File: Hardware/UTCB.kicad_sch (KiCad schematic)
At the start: 28 parts

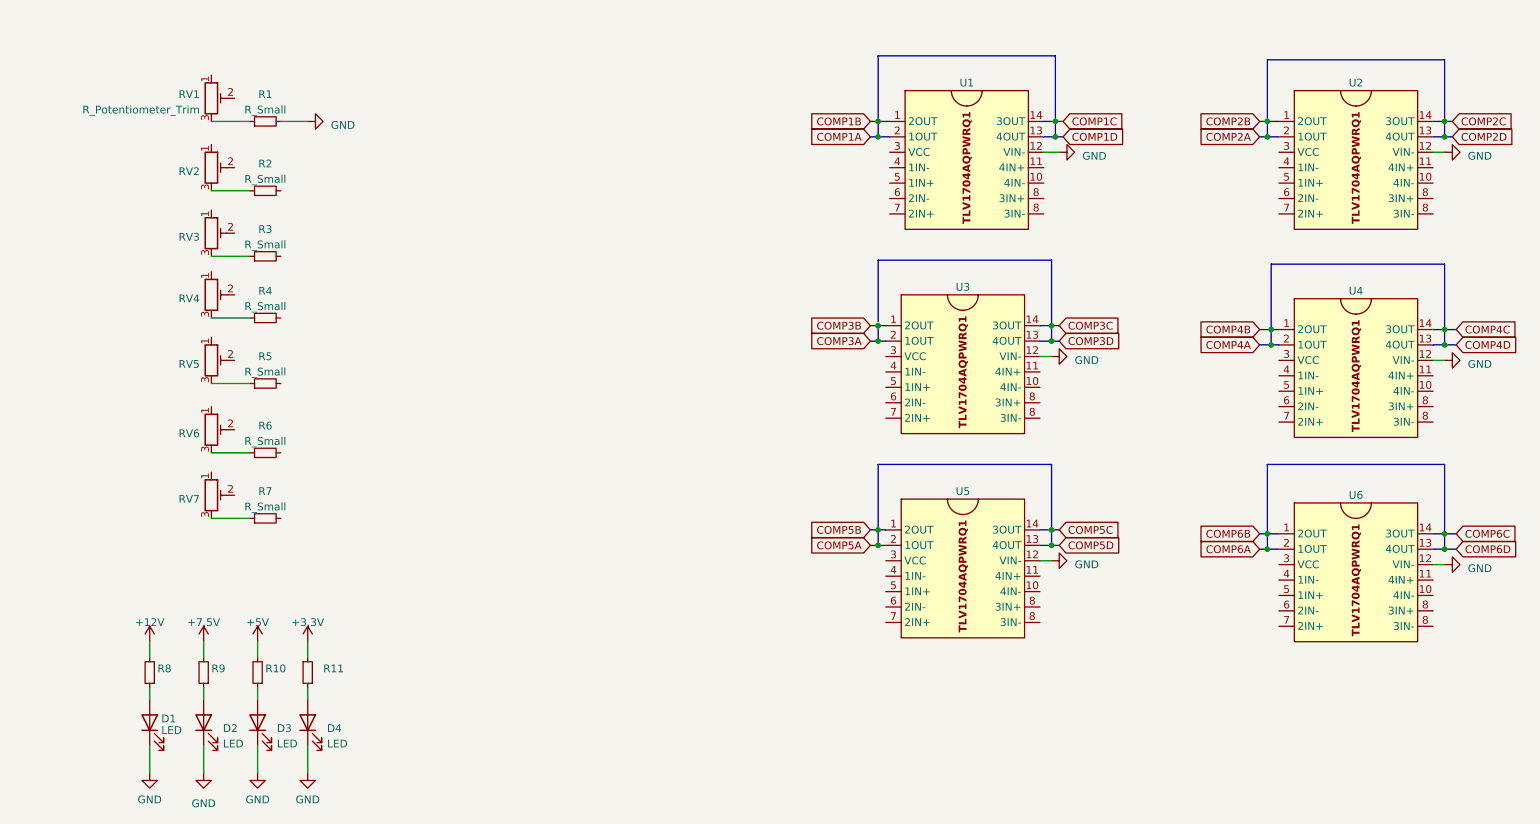
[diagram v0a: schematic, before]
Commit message: Added some changes for the logic switching circuitry. Will be adding thyristor or cascaded bjt configuration for various lighting types for each logic level
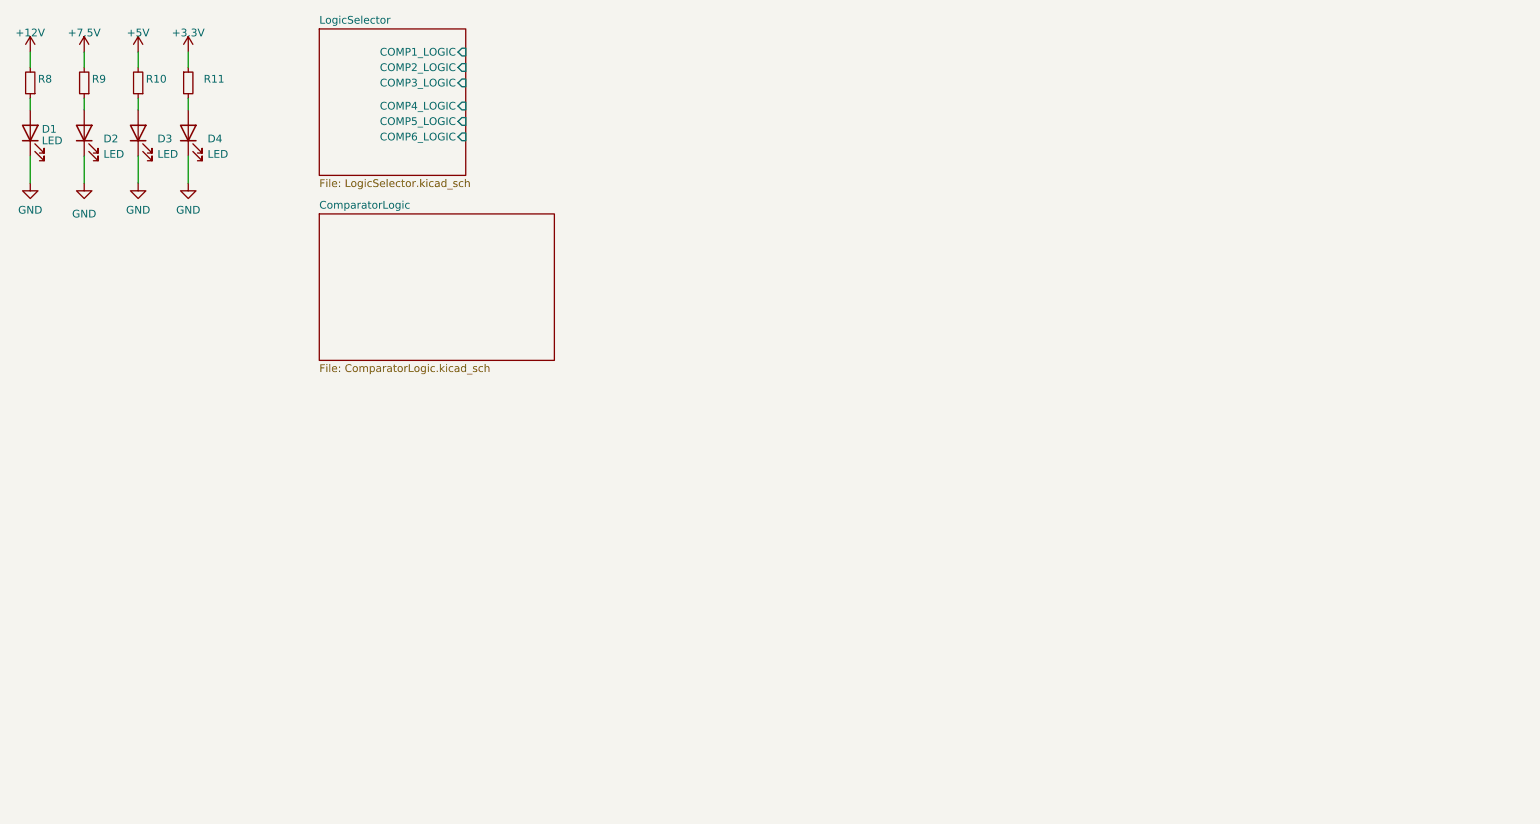
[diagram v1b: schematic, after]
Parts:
- removed R1, R2, R3, R4, R5, R6, R7: R_Small, symbol Device:R_Small
- removed RV1, RV2, RV3, RV4, RV5, RV6, RV7: R_Potentiometer_Trim, symbol Device:R_Potentiometer_Trim
- removed U1, U2, U3, U4, U5, U6: ~, Package_SO:HTSSOP-14-1EP_4.4x5mm_P0.65mm_EP3.4x5mm_Mask3x3.1mm, symbol ComparatorICs:TLV1704AQPWRQ1_
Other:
- added sheet ComparatorLogic (ComparatorLogic.kicad_sch)
- added sheet LogicSelector (LogicSelector.kicad_sch)
- moved on the sheet: D1, D2, D3, D4, R10, R11, R8, R9

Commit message: Added 3D models
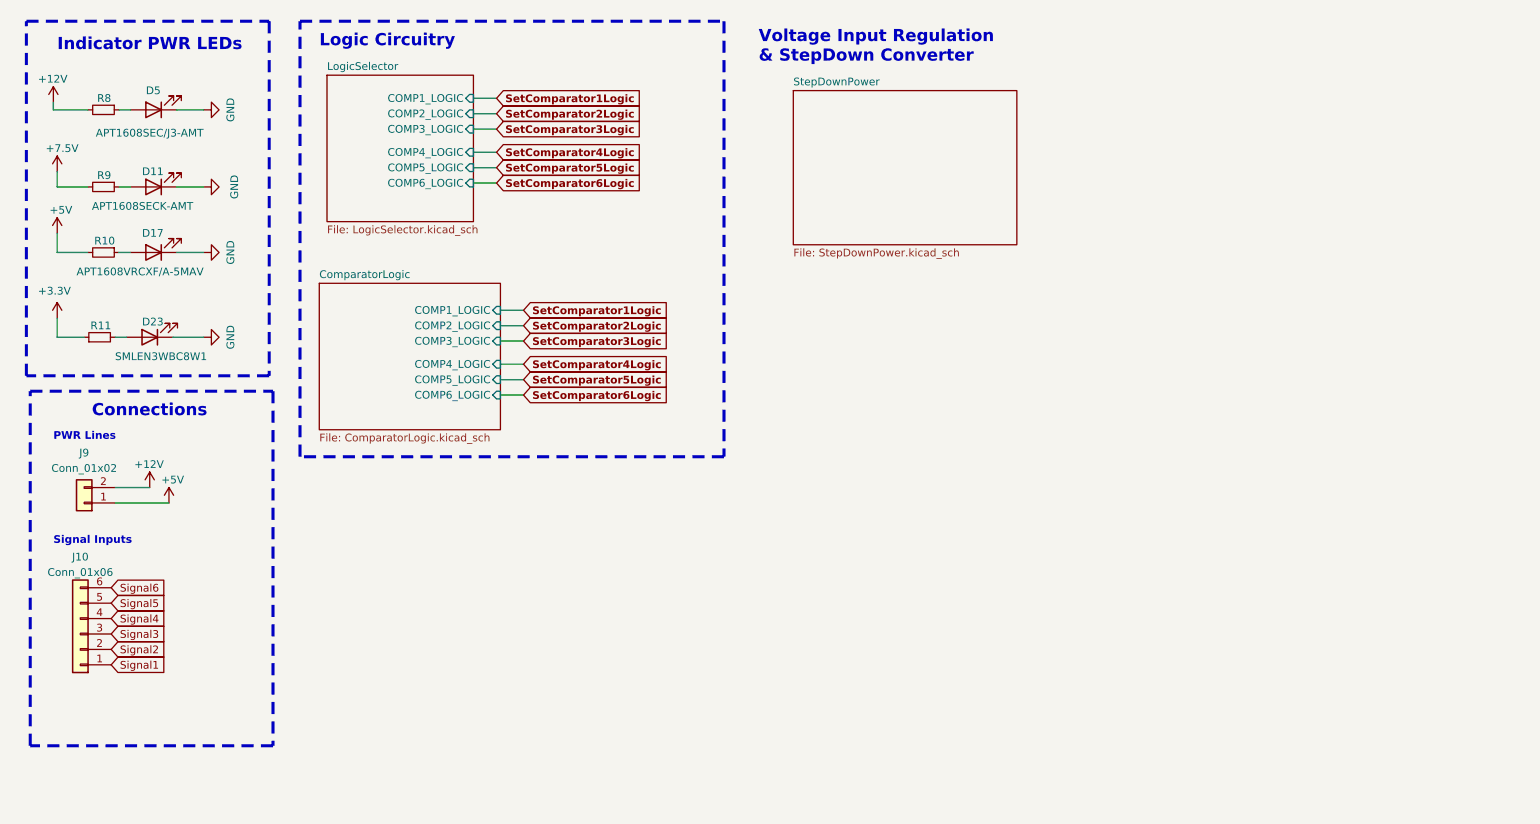
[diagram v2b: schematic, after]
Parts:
- removed D1, D2, D3, D4: LED, symbol Device:LED
- added D11: APT1608SECK-AMT, Diode_SMD:D_0603_1608Metric, symbol Device:LED
- added D17: APT1608VRCXF/A-5MAV, Diode_SMD:D_0603_1608Metric, symbol Device:LED
- added D23: SMLEN3WBC8W1, Diode_SMD:D_0603_1608Metric, symbol Device:LED
- added D5: APT1608SEC/J3-AMT, Diode_SMD:D_0603_1608Metric, symbol Device:LED
- added J10: Conn_01x06, Connector_PinHeader_1.27mm:PinHeader_1x06_P1.27mm_Vertical, symbol Connector_Generic:Conn_01x06
- added J9: Conn_01x02, Connector_PinHeader_1.27mm:PinHeader_1x02_P1.27mm_Vertical, symbol Connector_Generic:Conn_01x02
- R10, R11, R8, R9: footprint (none) -> Resistor_SMD:R_0603_1608Metric
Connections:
- net +12V: now also J9.2 (Pin_2)
- net +5V: now also J9.1 (Pin_1)
- net GND: now also D11.1 (K), D17.1 (K), D23.1 (K), D5.1 (K)
- net at R8.1: now also D5.2 (A)
- net at R10.1: now also D17.2 (A)
- net at R11.2: now also D23.2 (A)
- net at R9.1: now also D11.2 (A)
- new net Signal1: J10.1 (Pin_1)
- new net Signal2: J10.2 (Pin_2)
- new net Signal3: J10.3 (Pin_3)
- new net Signal4: J10.4 (Pin_4)
- new net Signal5: J10.5 (Pin_5)
- new net Signal6: J10.6 (Pin_6)
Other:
- added sheet StepDownPower (StepDownPower.kicad_sch)
- sheet ComparatorLogic ports: added COMP1_LOGIC, COMP2_LOGIC, COMP3_LOGIC, COMP4_LOGIC, COMP5_LOGIC, COMP6_LOGIC; removed none
- note added: "Connections"
- note added: "Indicator PWR LEDs"
- note added: "Logic Circuitry"
- note added: "PWR Lines"
- note added: "Signal Inputs"
- note added: "Voltage Input Regulation & StepDown Converter"
- moved on the sheet: R10, R11, R8, R9

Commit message: Added updates to logic switches for timing based logic. Updated attached 3D models.
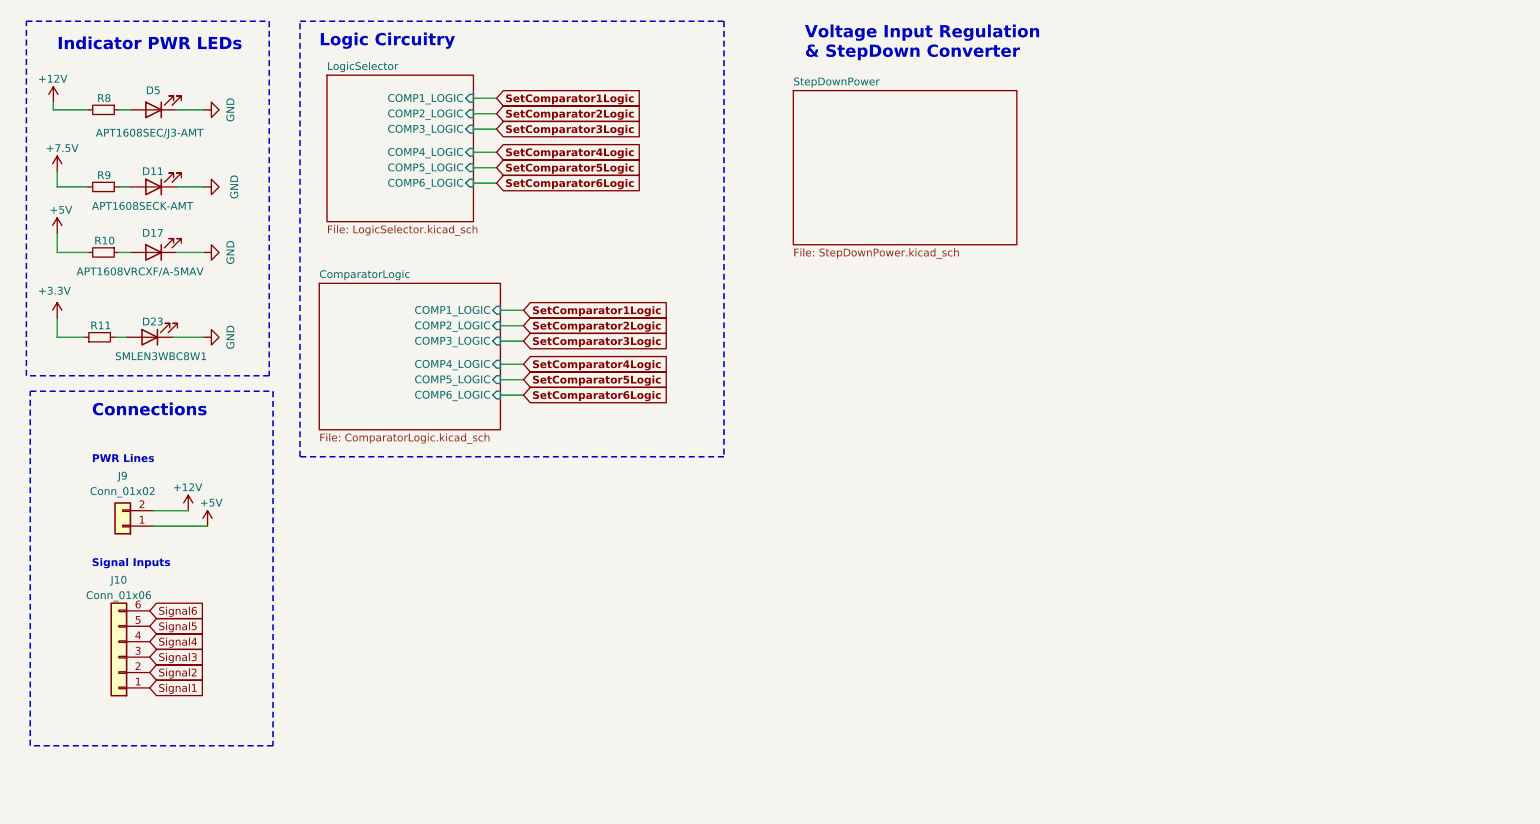
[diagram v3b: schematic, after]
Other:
- moved on the sheet: J10, J9
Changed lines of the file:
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@@
     (stroke (width 0) (type default))
   )
-  (wire (pts (xy 31.75 94.615) (xy 40.64 94.615))
+  (wire (pts (xy 38.1 98.425) (xy 46.99 98.425))
     (stroke (width 0) (type default))
   )
@@
     (stroke (width 0) (type default))
   )
-  (wire (pts (xy 31.75 92.075) (xy 37.465 92.075))
+  (wire (pts (xy 38.1 95.885) (xy 43.815 95.885))
     (stroke (width 0) (type default))
   )
@@
   )
   (rectangle (start 17.145 15.24) (end 57.15 73.66)
-    (stroke (width 0.5) (type dash_dot_dot))
+    (stroke (width 0.25) (type dash_dot_dot))
     (fill (type none))
   )
   (rectangle (start 62.23 15.24) (end 132.08 86.995)
-    (stroke (width 0.5) (type dash_dot_dot))
+    (stroke (width 0.25) (type dash_dot_dot))
     (fill (type none))
   )
   (rectangle (start 17.78 76.2) (end 57.785 134.62)
-    (stroke (width 0.5) (type dash_dot_dot))
+    (stroke (width 0.25) (type dash_dot_dot))
     (fill (type none))
   )
-  (text "PWR Lines" (at 21.59 84.455 0)
+  (text "PWR Lines" (at 27.94 88.265 0)
     (effects (font (size 1.27 1.27) (thickness 0.254) bold) (justify left bottom))
   )
@@
     (effects (font (size 2 2) bold) (justify left bottom))
   )
-  (text "Signal Inputs" (at 21.59 101.6 0)
+  (text "Signal Inputs" (at 27.94 105.41 0)
     (effects (font (size 1.27 1.27) (thickness 0.254) bold) (justify left bottom))
   )
@@
     (effects (font (size 2 2) bold) (justify left bottom))
   )
-  (text "Voltage Input Regulation\n& StepDown Converter" (at 137.795 22.225 0)
+  (text "Voltage Input Regulation\n& StepDown Converter" (at 145.415 21.59 0)
     (effects (font (size 2 2) bold) (justify left bottom))
   )
@@
     )
   )
-  (global_label "Signal4" (shape input) (at 31.115 113.665 0) (fields_autoplaced)
+  (global_label "Signal4" (shape input) (at 37.465 117.475 0) (fields_autoplaced)
     (effects (font (size 1.27 1.27)) (justify left))
-    (property "Intersheetrefs" "${INTERSHEET_REFS}" (at 41.1568 113.665 0)
-      (effects (font (size 1.27 1.27)) (justify left) hide)
-    )
-  )
-  (global_label "Signal3" (shape input) (at 31.115 116.205 0) (fields_autoplaced)
+    (property "Intersheetrefs" "${INTERSHEET_REFS}" (at 47.5068 117.475 0)
+      (effects (font (size 1.27 1.27)) (justify left) hide)
+    )
+  )
+  (global_label "Signal3" (shape input) (at 37.465 120.015 0) (fields_autoplaced)
     (effects (font (size 1.27 1.27)) (justify left))
-    (property "Intersheetrefs" "${INTERSHEET_REFS}" (at 41.1568 116.205 0)
-      (effects (font (size 1.27 1.27)) (justify left) hide)
-    )
-  )
-  (global_label "Signal6" (shape input) (at 31.115 108.585 0) (fields_autoplaced)
+    (property "Intersheetrefs" "${INTERSHEET_REFS}" (at 47.5068 120.015 0)
+      (effects (font (size 1.27 1.27)) (justify left) hide)
+    )
+  )
+  (global_label "Signal6" (shape input) (at 37.465 112.395 0) (fields_autoplaced)
     (effects (font (size 1.27 1.27)) (justify left))
-    (property "Intersheetrefs" "${INTERSHEET_REFS}" (at 0 0 0)
-      (effects (font (size 1.27 1.27)) hide)
-    )
-  )
-  (global_label "Signal1" (shape input) (at 31.115 121.285 0) (fields_autoplaced)
+    (property "Intersheetrefs" "${INTERSHEET_REFS}" (at 6.35 3.81 0)
+      (effects (font (size 1.27 1.27)) hide)
+    )
+  )
+  (global_label "Signal1" (shape input) (at 37.465 125.095 0) (fields_autoplaced)
     (effects (font (size 1.27 1.27)) (justify left))
-    (property "Intersheetrefs" "${INTERSHEET_REFS}" (at 0 15.875 0)
+    (property "Intersheetrefs" "${INTERSHEET_REFS}" (at 6.35 19.685 0)
       (effects (font (size 1.27 1.27)) hide)
     )
@@
     )
   )
-  (global_label "Signal5" (shape input) (at 31.115 111.125 0) (fields_autoplaced)
+  (global_label "Signal5" (shape input) (at 37.465 114.935 0) (fields_autoplaced)
     (effects (font (size 1.27 1.27)) (justify left))
-    (property "Intersheetrefs" "${INTERSHEET_REFS}" (at 41.1568 111.125 0)
+    (property "Intersheetrefs" "${INTERSHEET_REFS}" (at 47.5068 114.935 0)
       (effects (font (size 1.27 1.27)) (justify left) hide)
     )
@@
     )
   )
-  (global_label "Signal2" (shape input) (at 31.115 118.745 0) (fields_autoplaced)
+  (global_label "Signal2" (shape input) (at 37.465 122.555 0) (fields_autoplaced)
     (effects (font (size 1.27 1.27)) (justify left))
-    (property "Intersheetrefs" "${INTERSHEET_REFS}" (at 41.1568 118.745 0)
+    (property "Intersheetrefs" "${INTERSHEET_REFS}" (at 47.5068 122.555 0)
       (effects (font (size 1.27 1.27)) (justify left) hide)
     )
@@
     )
   )
-  (symbol (lib_id "power:+12V") (at 37.465 92.075 0) (unit 1)
-    (in_bom yes) (on_board yes) (dnp no)
-    (property "Reference" "#PWR0115" (at 37.465 95.885 0)
-      (effects (font (size 1.27 1.27)) hide)
-    )
-    (property "Value" "+12V" (at 34.925 88.265 0)
+  (symbol (lib_id "power:+12V") (at 43.815 95.885 0) (unit 1)
+    (in_bom yes) (on_board yes) (dnp no)
+    (property "Reference" "#PWR0115" (at 43.815 99.695 0)
+      (effects (font (size 1.27 1.27)) hide)
+    )
+    (property "Value" "+12V" (at 41.275 92.075 0)
       (effects (font (size 1.27 1.27)) (justify left))
     )
-    (property "Footprint" "" (at 37.465 92.075 0)
-      (effects (font (size 1.27 1.27)) hide)
-    )
-    (property "Datasheet" "" (at 37.465 92.075 0)
+    (property "Footprint" "" (at 43.815 95.885 0)
+      (effects (font (size 1.27 1.27)) hide)
+    )
+    (property "Datasheet" "" (at 43.815 95.885 0)
       (effects (font (size 1.27 1.27)) hide)
     )
@@
     )
   )
-  (symbol (lib_id "power:+5V") (at 40.64 94.615 0) (unit 1)
-    (in_bom yes) (on_board yes) (dnp no)
-    (property "Reference" "#PWR0116" (at 40.64 98.425 0)
-      (effects (font (size 1.27 1.27)) hide)
-    )
-    (property "Value" "+5V" (at 39.37 90.805 0)
+  (symbol (lib_id "power:+5V") (at 46.99 98.425 0) (unit 1)
+    (in_bom yes) (on_board yes) (dnp no)
+    (property "Reference" "#PWR0116" (at 46.99 102.235 0)
+      (effects (font (size 1.27 1.27)) hide)
+    )
+    (property "Value" "+5V" (at 45.72 94.615 0)
       (effects (font (size 1.27 1.27)) (justify left))
     )
-    (property "Footprint" "" (at 40.64 94.615 0)
-      (effects (font (size 1.27 1.27)) hide)
-    )
-    (property "Datasheet" "" (at 40.64 94.615 0)
+    (property "Footprint" "" (at 46.99 98.425 0)
+      (effects (font (size 1.27 1.27)) hide)
+    )
+    (property "Datasheet" "" (at 46.99 98.425 0)
       (effects (font (size 1.27 1.27)) hide)
     )
@@
     )
   )
-  (symbol (lib_id "Connector_Generic:Conn_01x02") (at 26.67 94.615 180) (unit 1)
-    (in_bom yes) (on_board yes) (dnp no)
-    (property "Reference" "J9" (at 26.67 86.36 0)
-      (effects (font (size 1.27 1.27)))
-    )
-    (property "Value" "Conn_01x02" (at 26.67 88.9 0)
-      (effects (font (size 1.27 1.27)))
-    )
-    (property "Footprint" "Connector_PinHeader_1.27mm:PinHeader_1x02_P1.27mm_Vertical" (at 26.67 94.615 0)
-      (effects (font (size 1.27 1.27)) hide)
-    )
-    (property "Datasheet" "~" (at 26.67 94.615 0)
+  (symbol (lib_id "Connector_Generic:Conn_01x02") (at 33.02 98.425 180) (unit 1)
+    (in_bom yes) (on_board yes) (dnp no)
+    (property "Reference" "J9" (at 33.02 90.17 0)
+      (effects (font (size 1.27 1.27)))
+    )
+    (property "Value" "Conn_01x02" (at 33.02 92.71 0)
+      (effects (font (size 1.27 1.27)))
+    )
+    (property "Footprint" "Connector_PinHeader_1.27mm:PinHeader_1x02_P1.27mm_Vertical" (at 33.02 98.425 0)
+      (effects (font (size 1.27 1.27)) hide)
+    )
+    (property "Datasheet" "~" (at 33.02 98.425 0)
       (effects (font (size 1.27 1.27)) hide)
     )
@@
     )
   )
-  (symbol (lib_id "Connector_Generic:Conn_01x06") (at 26.035 116.205 180) (unit 1)
+  (symbol (lib_id "Connector_Generic:Conn_01x06") (at 32.385 120.015 180) (unit 1)
     (in_bom yes) (on_board yes) (dnp no) (fields_autoplaced)
-    (property "Reference" "J10" (at 26.035 103.505 0)
-      (effects (font (size 1.27 1.27)))
-    )
-    (property "Value" "Conn_01x06" (at 26.035 106.045 0)
-      (effects (font (size 1.27 1.27)))
-    )
-    (property "Footprint" "Connector_PinHeader_1.27mm:PinHeader_1x06_P1.27mm_Vertical" (at 26.035 116.205 0)
-      (effects (font (size 1.27 1.27)) hide)
-    )
-    (property "Datasheet" "~" (at 26.035 116.205 0)
-      (effects (font (size 1.27 1.27)) hide)
-    )
+    (property "Reference" "J10" (at 32.385 107.315 0)
+      (effects (font (size 1.27 1.27)))
+    )
+    (property "Value" "Conn_01x06" (at 32.385 109.855 0)
+      (effects (font (size 1.27 1.27)))
+    )
+    (property "Footprint" "Connector_PinHeader_1.27mm:PinHeader_1x06_P1.27mm_Vertical" (at 32.385 120.015 0)
+      (effects (font (size 1.27 1.27)) hide)
+    )
+    (property "Datasheet" "~" (at 32.385 120.015 0)
+      (effects (font (size 1.27 1.27)) hide)
+    )
